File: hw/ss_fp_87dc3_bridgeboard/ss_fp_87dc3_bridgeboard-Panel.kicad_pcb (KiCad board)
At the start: 2 copper layers, 50 x 40 mm, 32 parts, among them J101 Conn_01x02, J102 Conn_01x04, J103 Conn_01x03, J104 Conn_01x02, J105 Conn_01x04, J106 Conn_01x03, J107 Conn_01x02, J108 Conn_01x04, J109 Conn_01x02, J110 Conn_01x04, J111 Conn_01x03, J112 Conn_01x03

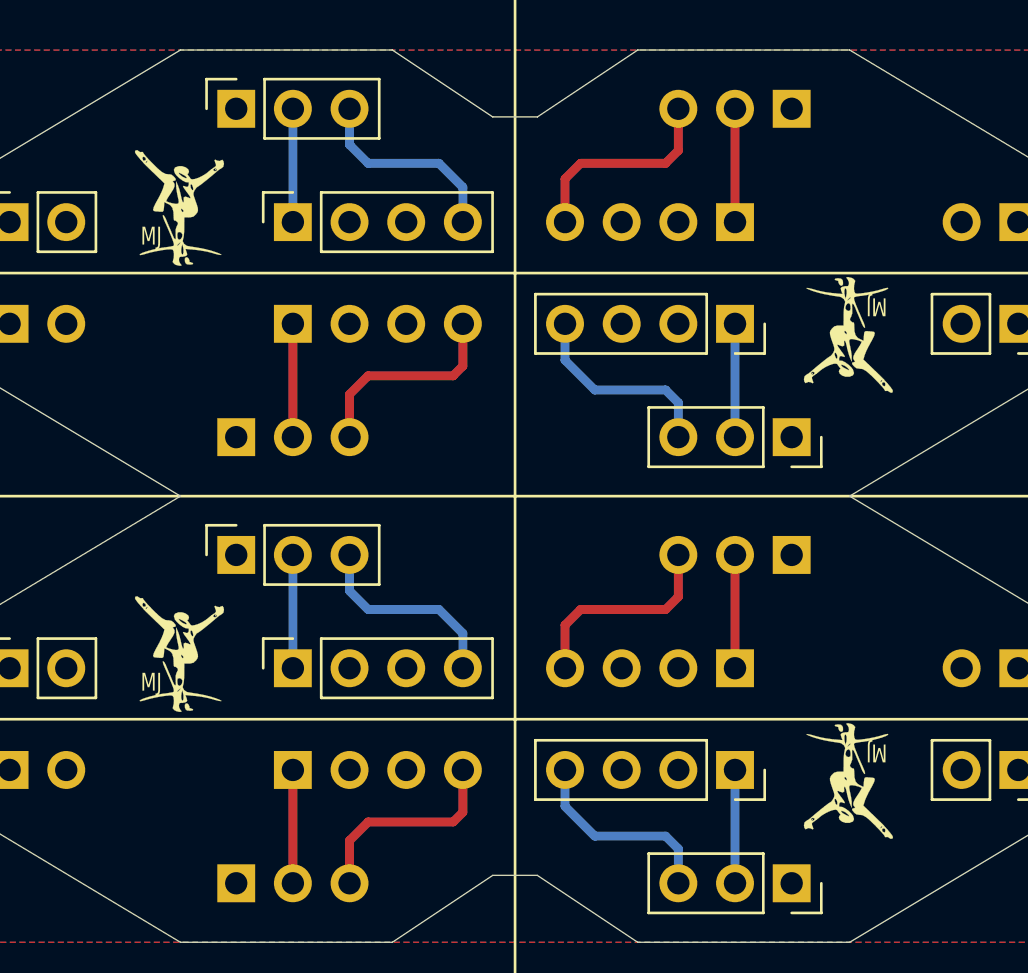
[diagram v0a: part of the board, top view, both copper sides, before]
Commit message: Bridge board: add placeholder JLC serial label in silk
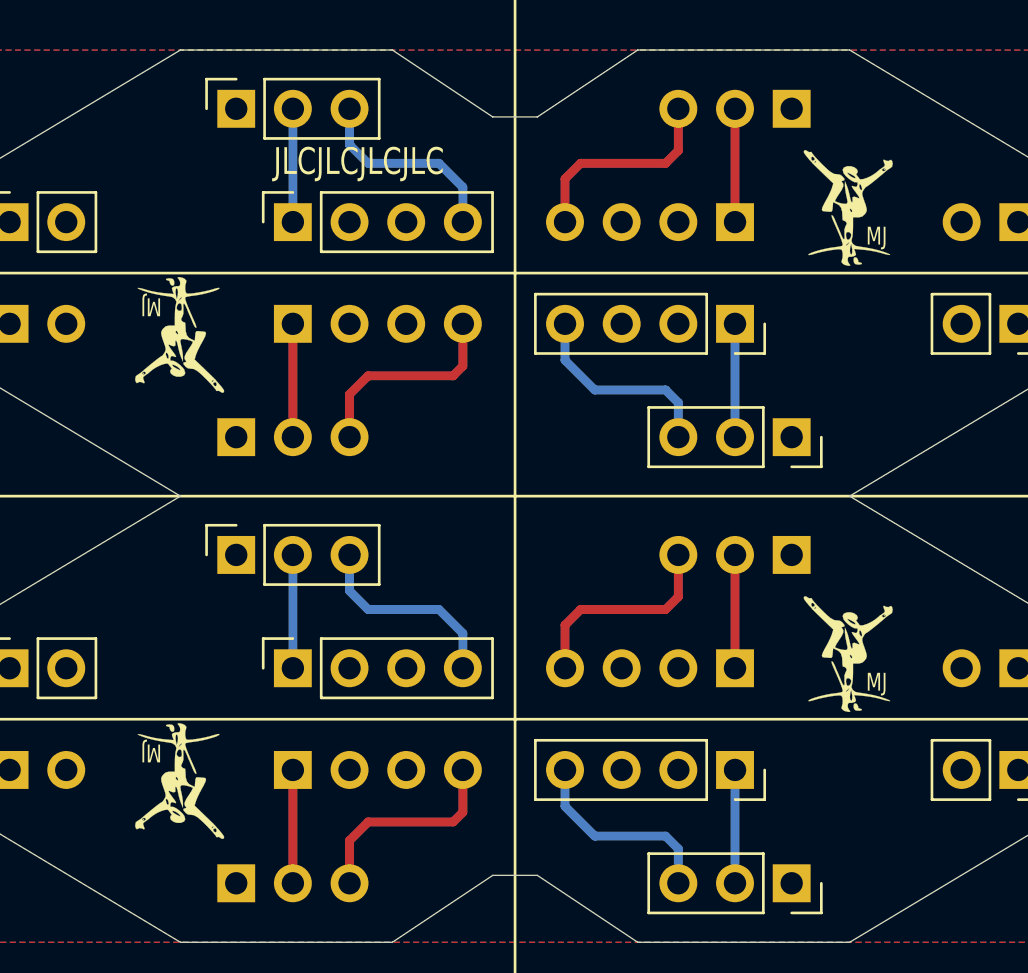
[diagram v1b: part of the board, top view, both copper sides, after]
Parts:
- Logo101 (x2), Logo104 (x2): moved to B.Cu
- Logo102 (x2), Logo103 (x2): moved to F.Cu
- turned Logo101 to 180 degrees (x2)
- turned Logo102 to 0 degrees (x2)
- turned Logo103 to 180 degrees (x2)
- turned Logo104 to 0 degrees (x2)
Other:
- board text added: "JLCJLCJLCJLC"

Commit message: Kicad 6.0 : Most of SS2k & subprojects updated to kicad6 The projects should from now on be opened through the .kicad_pro files instead of .pro, etc. NOTE: Kicad 6 is now used. Kicad5 is NOT able to open v6+ files.
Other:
- net class Default removed
